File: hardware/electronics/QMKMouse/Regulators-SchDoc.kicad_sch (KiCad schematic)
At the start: 9 parts

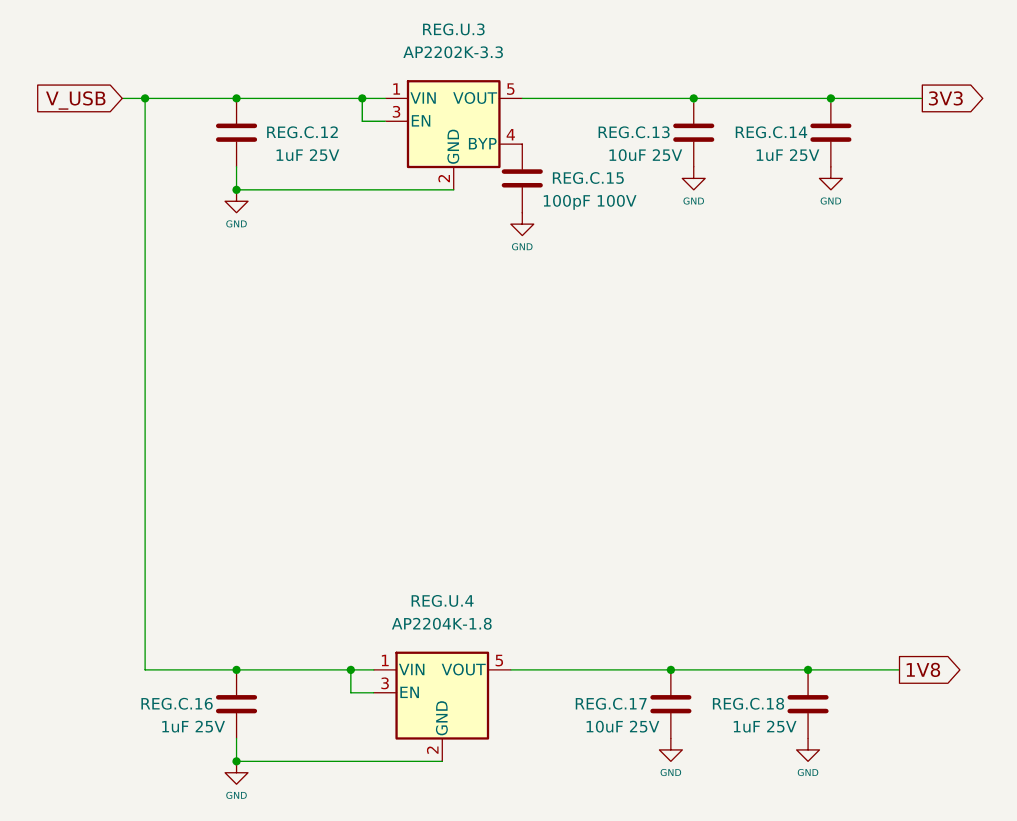
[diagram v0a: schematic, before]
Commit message: fix ERC errors and use hierarchy labels
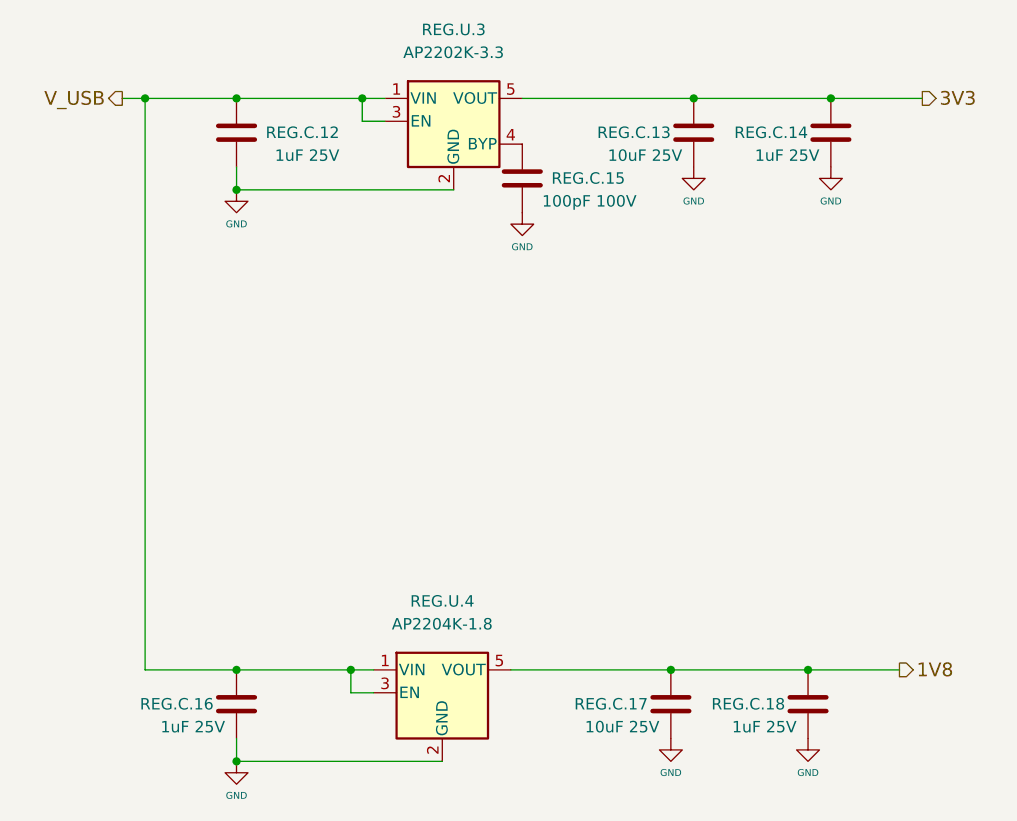
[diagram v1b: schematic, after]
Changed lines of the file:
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@@
     (stroke (width 0) (type default) (color 0 0 0 0))
   )
-  (global_label "1V8" (shape output) (at 165.1 132.08 0) (fields_autoplaced)
+  (hierarchical_label "V_USB" (shape output) (at 78.74 68.58 180)
+    (effects (font (size 1.524 1.524)) (justify right))
+  )
+  (hierarchical_label "1V8" (shape output) (at 165.1 132.08 0)
     (effects (font (size 1.524 1.524)) (justify left))
-    (property "Intersheet References" "${INTERSHEET_REFS}" (id 0) (at -20.32 -63.5 0)
-      (effects (font (size 1.27 1.27)) hide)
-    )
   )
-  (global_label "3V3" (shape output) (at 167.64 68.58 0) (fields_autoplaced)
+  (hierarchical_label "3V3" (shape output) (at 167.64 68.58 0)
     (effects (font (size 1.524 1.524)) (justify left))
-    (property "Intersheet References" "${INTERSHEET_REFS}" (id 0) (at -17.78 -63.5 0)
-      (effects (font (size 1.27 1.27)) hide)
-    )
-  )
-  (global_label "V_USB" (shape input) (at 78.74 68.58 180) (fields_autoplaced)
-    (effects (font (size 1.524 1.524)) (justify right))
-    (property "Intersheet References" "${INTERSHEET_REFS}" (id 0) (at 152.4 -63.5 0)
-      (effects (font (size 1.27 1.27)) (justify left) hide)
-    )
   )
   (symbol (lib_id "power:GND") (at 154.94 139.7 0) (unit 1)

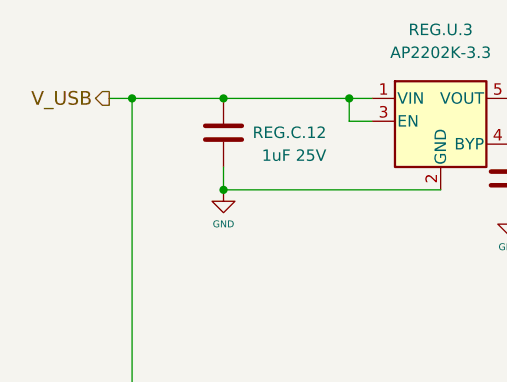
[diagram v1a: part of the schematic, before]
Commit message: Fix all ERC errors and replot the schematic
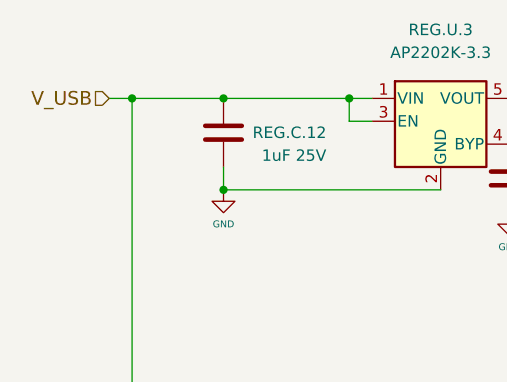
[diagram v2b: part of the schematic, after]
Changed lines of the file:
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@@
-    (stroke (width 0) (type default) (color 0 0 0 0))
-  )
-  (wire (pts (xy 91.44 78.74) (xy 115.57 78.74))
     (stroke (width 0) (type default) (color 0 0 0 0))
   )
@@
     (stroke (width 0) (type default) (color 0 0 0 0))
   )
+  (wire (pts (xy 91.44 78.74) (xy 115.57 78.74))
+    (stroke (width 0) (type default) (color 0 0 0 0))
+  )
   (wire (pts (xy 81.28 68.58) (xy 91.44 68.58))
     (stroke (width 0) (type default) (color 0 0 0 0))
@@
     (stroke (width 0) (type default) (color 0 0 0 0))
   )
-  (hierarchical_label "V_USB" (shape output) (at 78.74 68.58 180)
+  (hierarchical_label "V_USB" (shape input) (at 78.74 68.58 180)
     (effects (font (size 1.524 1.524)) (justify right))
   )

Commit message: reference 3d model to all components
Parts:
- REG.C.12, REG.C.13, REG.C.14, REG.C.15, REG.C.16, REG.C.17, REG.C.18: footprint Chip_Passives.PcbLib:0805 -> mouse_part:C_0805
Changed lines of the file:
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@@
       (effects (font (size 1.27 1.27)) (justify right))
     )
-    (property "Footprint" "Chip_Passives.PcbLib:0805" (id 2) (at 143.2052 68.58 0)
+    (property "Footprint" "mouse_part:C_0805" (id 2) (at 143.2052 68.58 0)
       (effects (font (size 1.27 1.27)) hide)
     )
@@
       (effects (font (size 1.27 1.27)) (justify right))
     )
-    (property "Footprint" "Chip_Passives.PcbLib:0805" (id 2) (at 92.4052 132.08 0)
+    (property "Footprint" "mouse_part:C_0805" (id 2) (at 92.4052 132.08 0)
       (effects (font (size 1.27 1.27)) hide)
     )
@@
       (effects (font (size 1.27 1.27)) (justify right))
     )
-    (property "Footprint" "Chip_Passives.PcbLib:0805" (id 2) (at 140.6652 132.08 0)
+    (property "Footprint" "mouse_part:C_0805" (id 2) (at 140.6652 132.08 0)
       (effects (font (size 1.27 1.27)) hide)
     )
@@
       (effects (font (size 1.27 1.27)) (justify right))
     )
-    (property "Footprint" "Chip_Passives.PcbLib:0805" (id 2) (at 155.9052 132.08 0)
+    (property "Footprint" "mouse_part:C_0805" (id 2) (at 155.9052 132.08 0)
       (effects (font (size 1.27 1.27)) hide)
     )
@@
       (effects (font (size 1.27 1.27)) (justify right))
     )
-    (property "Footprint" "Chip_Passives.PcbLib:0805" (id 2) (at 158.4452 68.58 0)
+    (property "Footprint" "mouse_part:C_0805" (id 2) (at 158.4452 68.58 0)
       (effects (font (size 1.27 1.27)) hide)
     )
@@
       (effects (font (size 1.27 1.27)) (justify right))
     )
-    (property "Footprint" "Chip_Passives.PcbLib:0805" (id 2) (at 124.1552 73.66 0)
+    (property "Footprint" "mouse_part:C_0805" (id 2) (at 124.1552 73.66 0)
       (effects (font (size 1.27 1.27)) hide)
     )
@@
       (effects (font (size 1.27 1.27)) (justify right))
     )
-    (property "Footprint" "Chip_Passives.PcbLib:0805" (id 2) (at 92.4052 68.58 0)
+    (property "Footprint" "mouse_part:C_0805" (id 2) (at 92.4052 68.58 0)
       (effects (font (size 1.27 1.27)) hide)
     )
